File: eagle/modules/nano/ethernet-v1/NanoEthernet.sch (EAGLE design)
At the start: 55 parts, among them IC1 ULN2803A, IC2 ULN2803A, IC4 ULN2803A, J1 RJ12STRAIGHT-RS232-SERVER

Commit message: New NanoEthernet version (draft)
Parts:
- removed IC1, IC4: ULN2803A, lpatiny:ULN2803A
- removed RA3, RA6, RA7: 10K, resistor:R-EU_M1206
- removed RGB1_D5-6-11: RGB1, lpatiny:RJ12STRAIGHT-RGB
- removed RGB2_D7-8-13: RGB2, lpatiny:RJ12STRAIGHT-RGB
- removed RGB_5-6-11, RGB_7-8-13: (no value), lpatiny:TOPLED-3
- removed RL11, RL13, RL5, RL6, RL7, RL8: 1K, resistor:R-EU_M1206
- added A1, A2: RJ12STRAIGHT-ANALOG, lpatiny:RJ12STRAIGHT-ANALOG
- added CON1: (no value), lpatiny:CON10EXT
- added LED5: LED3MM, lpatiny:LED3MM
- added RA0, RA1, RL14: 1K, resistor:R-EU_M1206
- added SG2: F/HMB, buzzer:F/HMB
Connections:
- removed net N$1: RGB_5-6-11.CRED, RL5.2
- removed net N$11: RGB_7-8-13.CBLUE, RL8.2
- removed net N$14: RGB_7-8-13.CGREEN, RL13.2
- removed net N$17: IC4.O5, IC4.O6, RGB1_D5-6-11.4, RL11.1
- removed net N$19: IC4.O7, IC4.O8, RGB2_D7-8-13.2, RL7.1
- removed net N$2: RGB_5-6-11.CBLUE, RL6.2
- removed net N$29: IC1.O3, IC1.O4, RGB2_D7-8-13.4, RL13.1
- removed net N$3: IC1.O1, IC1.O2, RGB2_D7-8-13.3, RL8.1
- removed net N$4: RGB_5-6-11.CGREEN, RL11.2
- removed net N$5: IC4.O1, IC4.O2, RGB1_D5-6-11.2, RL5.1
- removed net N$6: IC4.O3, IC4.O4, RGB1_D5-6-11.3, RL6.1
- removed net N$9: RGB_7-8-13.CRED, RL7.2
- new net D2B8: A1.3, RA0.1
- new net D2B9: A2.3, RA1.1
- new net N$10: LED5.A, RL14.1
- net +12V: now also A1.1, A2.1; no longer RGB1_D5-6-11.1, RGB2_D7-8-13.1
- net +5V: now also A1.5, A2.5; no longer RGB1_D5-6-11.5, RGB2_D7-8-13.5, RGB_5-6-11.A2, RGB_7-8-13.A2
- net A1: now also RA0.2
- net A2: now also RA1.2
- net COM: no longer IC1.CD+, IC4.CD+
- net D11: no longer IC4.I1, IC4.I2
- net D13: no longer IC1.I3, IC1.I4
- net D2: no longer IC1.I5, IC1.I6
- net D3: no longer IC1.I7, IC1.I8
- net D4: no longer IC2.I1, IC2.I2
- net D5: no longer IC4.I5, IC4.I6
- net D6: no longer IC4.I3, IC4.I4
- net D7: no longer IC4.I7, IC4.I8
- net D8: no longer IC1.I1, IC1.I2
- net D9: no longer IC2.I3, IC2.I4
- net GND: now also A1.2, A1.4, A1.6, A2.2, A2.4, A2.6, LED5.C, SG2.-; no longer IC1.GND, IC4.GND, RA3.2, RA6.2, RA7.2, RGB1_D5-6-11.6, RGB2_D7-8-13.6
- net N$16: no longer RA3.1
- net N$18: now also IC2.O3; no longer IC2.O1, IC2.O2
- net N$20: now also RL14.2; no longer RA6.1
- net N$22: now also SG2.+; no longer RA7.1
- net N$35: now also IC2.O2; no longer IC1.O7, IC1.O8
- net N$40: no longer IC1.O5, IC1.O6
- net N$42: no longer IC2.O3
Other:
- moved on the sheet: D2, IC2

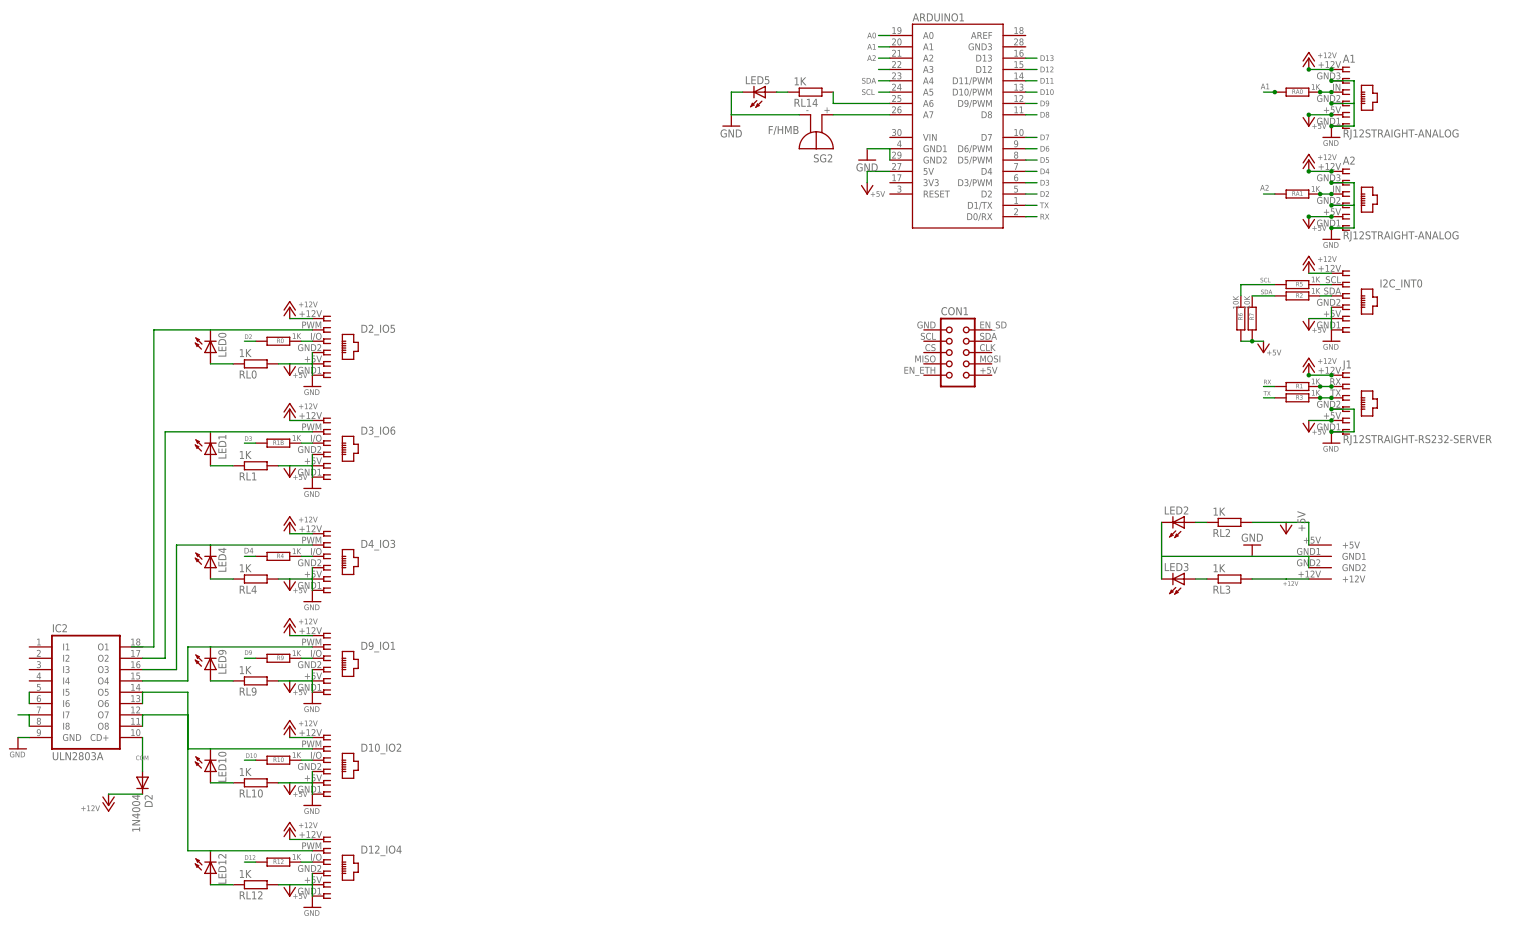
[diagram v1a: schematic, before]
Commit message: update ethernet card
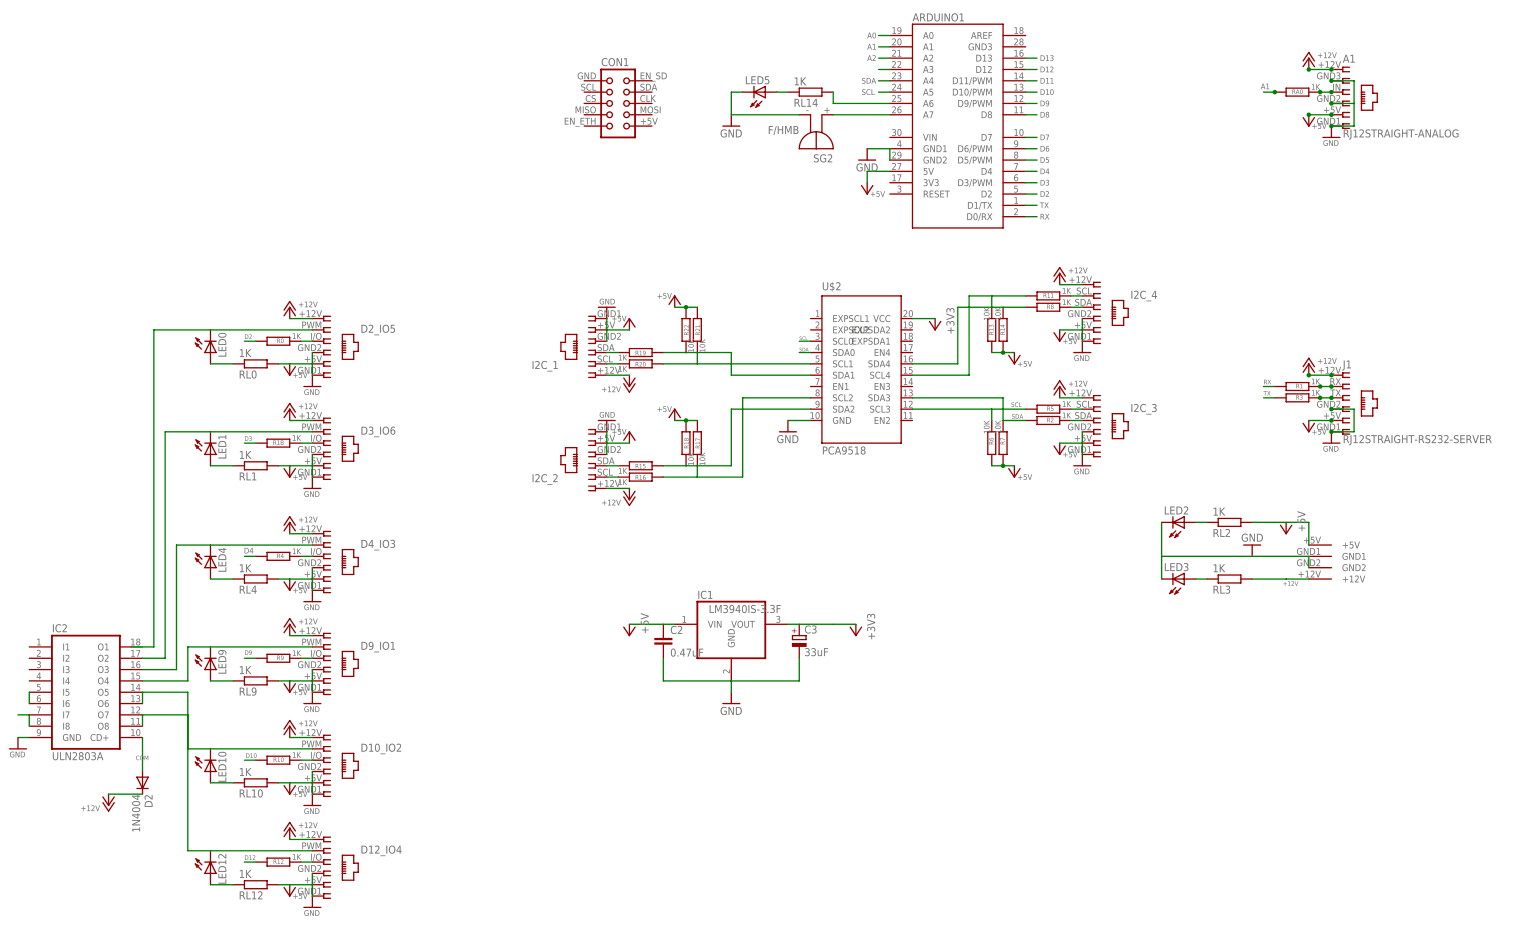
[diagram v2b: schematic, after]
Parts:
- removed A2: RJ12STRAIGHT-ANALOG, lpatiny:RJ12STRAIGHT-ANALOG
- removed I2C_INT0: I2C, lpatiny:RJ12STRAIGHT-I2C
- removed RA1: 1K, resistor:R-EU_M1206
- added C2: 0.47uF, rcl:C-EUC1206
- added C3: 33uF, rcl:CPOL-EUE3.5-8
- added I2C_1, I2C_2, I2C_3, I2C_4: I2C, lpatiny:RJ12STRAIGHT-I2C
- added IC1: LM3940IS-3.3F, lpatiny:LM3940IS-3.3F
- added R11, R15, R16, R19, R20, R8: 1K, resistor:R-EU_M1206
- added R13, R14, R17, R18, R21, R22: 10K, resistor:R-EU_M1206
- added U$2: PCA9518, lpatiny:PCA9518
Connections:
- removed net D2B9: A2.3, RA1.1
- new net +3V3: C3.+, IC1.VOUT, U$2.VCC
- new net D2B10: I2C_4.3, R8.1
- new net D2B11: I2C_2.3, R15.1
- new net D2B12: I2C_1.3, R19.1
- new net N$1: I2C_4.2, R11.1
- new net N$11: I2C_1.2, R20.1
- new net N$14: R20.2, R21.1, U$2.SCL1
- new net N$17: R19.2, R22.1, U$2.SDA1
- new net N$2: R11.2, R13.1, U$2.SCL4
- new net N$3: R14.1, R8.2, U$2.SDA4
- new net N$5: I2C_2.2, R16.1
- new net N$6: R16.2, R17.1, U$2.SCL2
- new net N$9: R15.2, R18.1, U$2.SDA2
- net +12V: now also I2C_1.1, I2C_2.1, I2C_3.1, I2C_4.1; no longer A2.1, I2C_INT0.1
- net +5V: now also C2.1, I2C_1.5, I2C_2.5, I2C_3.5, I2C_4.5, IC1.VIN, R13.2, R14.2, R17.2, R18.2, R21.2, R22.2; no longer A2.5, I2C_INT0.5
- net A2: no longer RA1.2
- net D2B4: now also I2C_3.3; no longer I2C_INT0.3
- net GND: now also C2.2, C3.-, I2C_1.4, I2C_1.6, I2C_2.4, I2C_2.6, I2C_3.4, I2C_3.6, I2C_4.4, I2C_4.6, IC1.GND, U$2.GND; no longer A2.2, A2.4, A2.6, I2C_INT0.4, I2C_INT0.6
- net N$8: now also I2C_3.2; no longer I2C_INT0.2
- net SCL: now also U$2.SCL0, U$2.SCL3
- net SDA: now also U$2.SDA0, U$2.SDA3
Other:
- moved on the sheet: CON1, R2, R5, R6, R7
